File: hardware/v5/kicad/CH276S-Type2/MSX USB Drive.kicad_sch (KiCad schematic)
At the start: 11 parts, among them J1 AVR-JTAG-10, J2 Conn_02x08_Odd_Even, SW1 SK12D07VG4, U1 EPM7064STC44-7, U2 SST39SF040

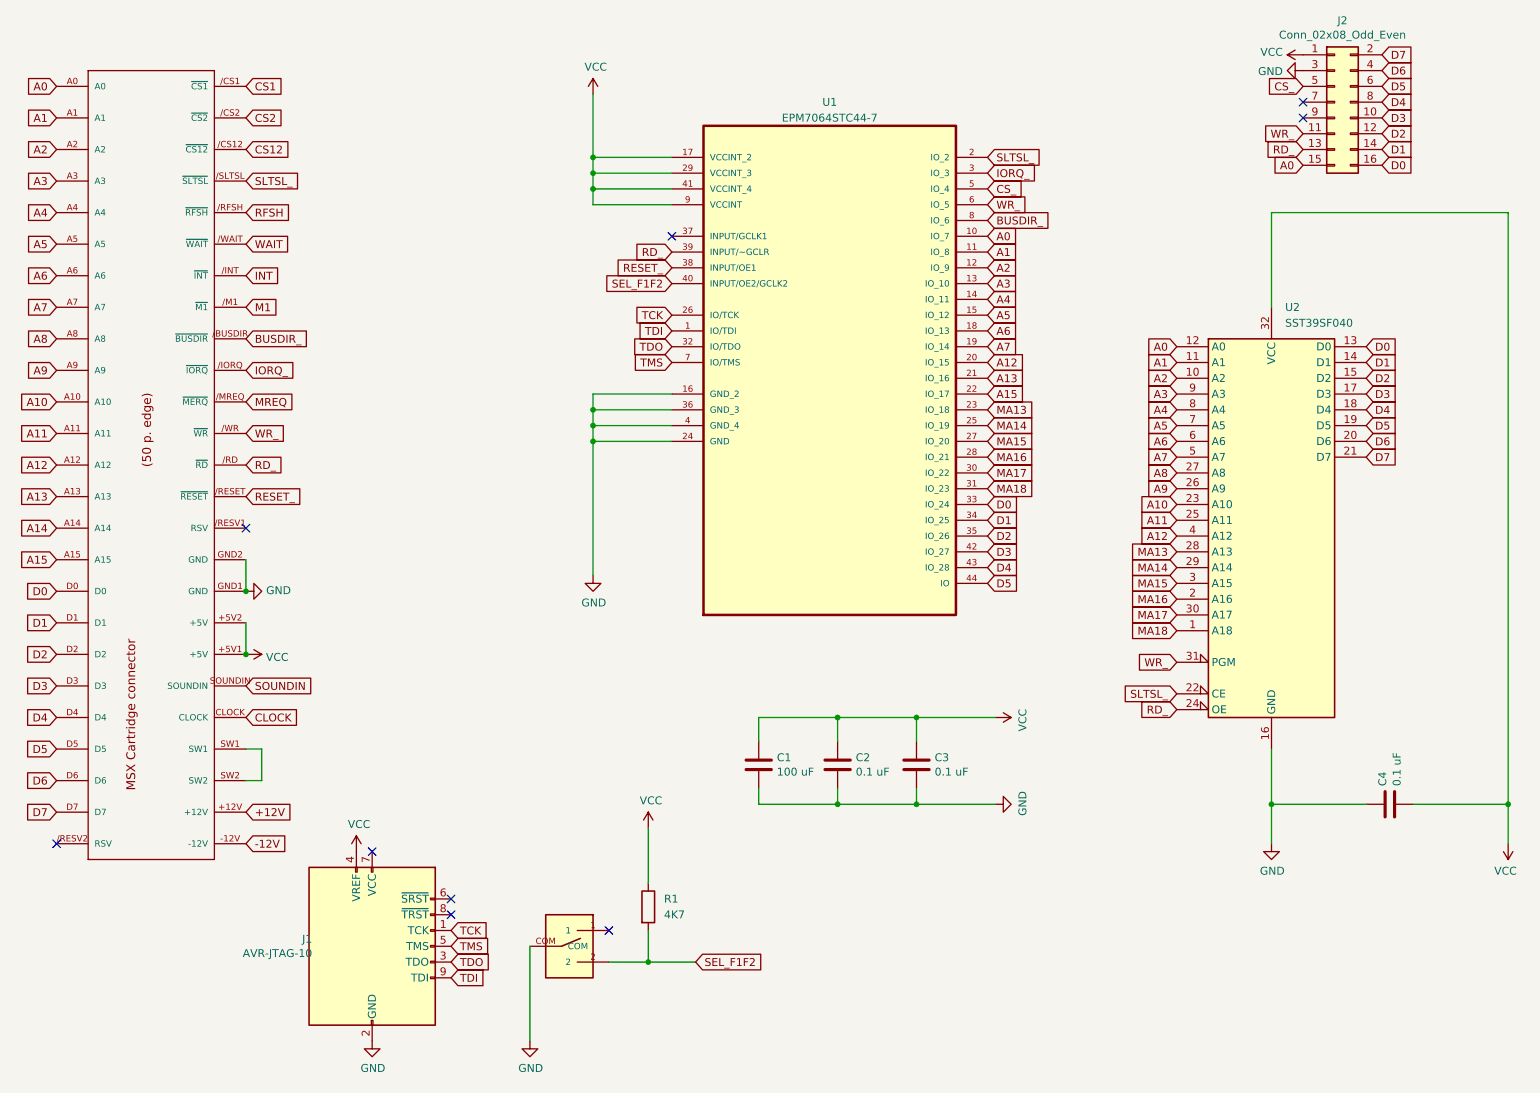
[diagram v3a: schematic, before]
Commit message: fix flash tool, adjustments to v5 pcbs, tests with fusion-c
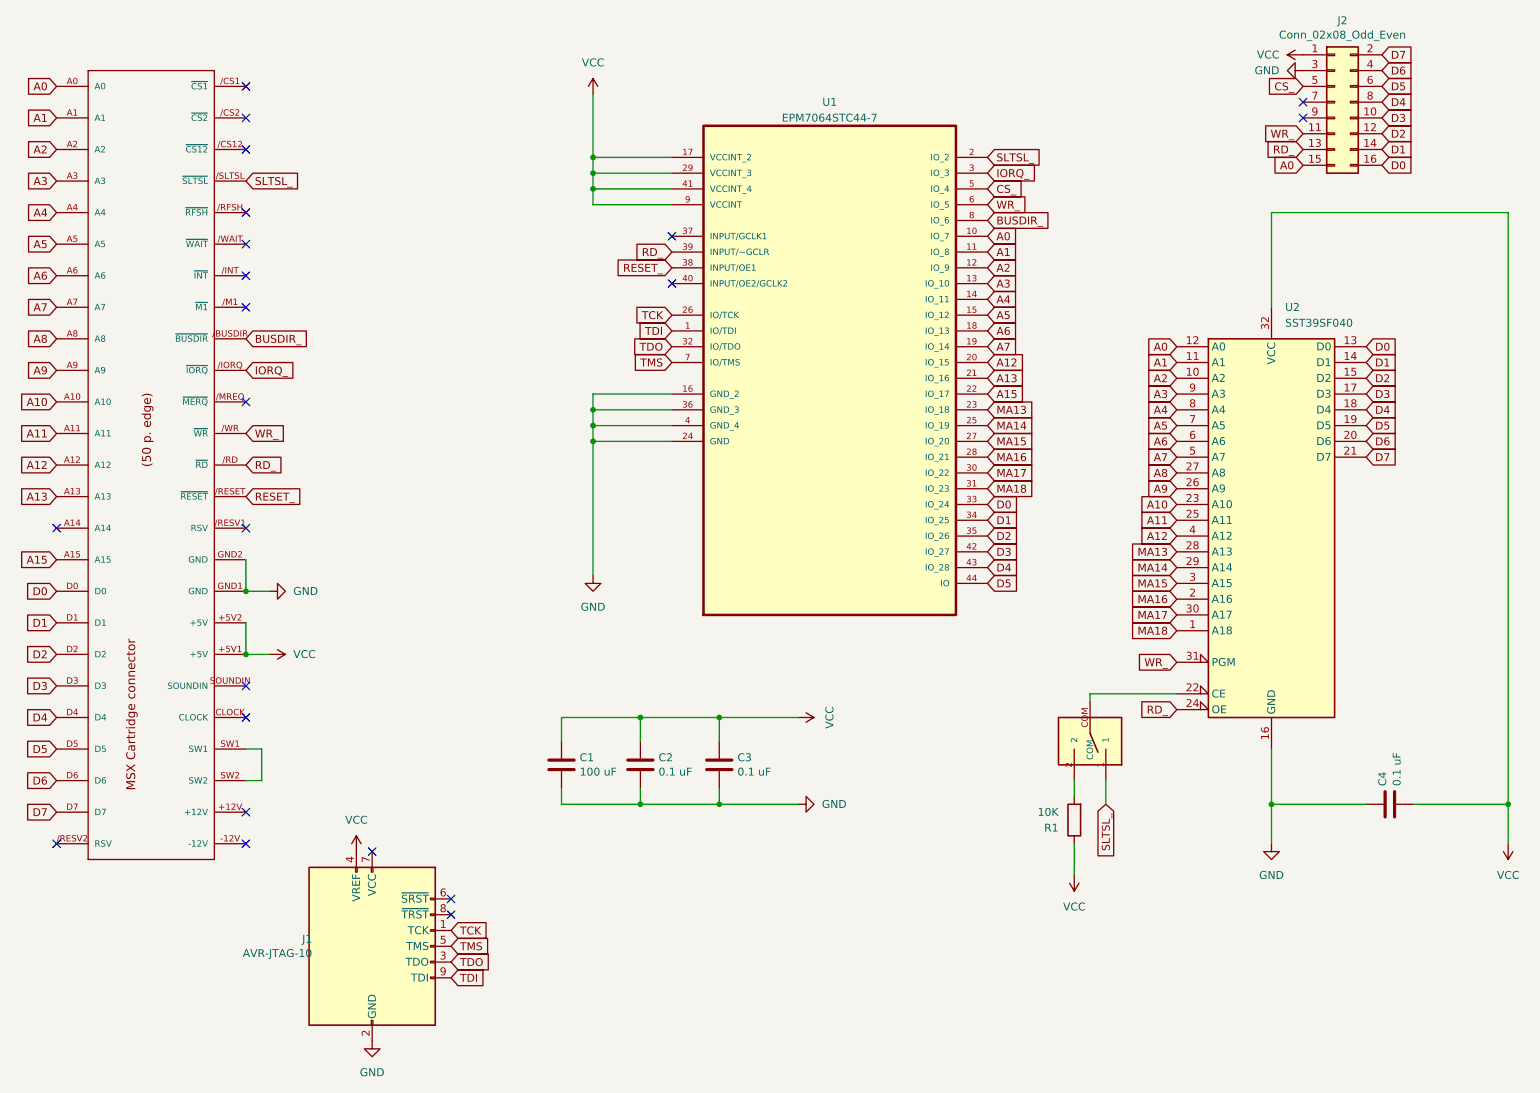
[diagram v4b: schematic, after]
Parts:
- R1: value 4K7 -> 10K
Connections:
- net GND: no longer SW1.COM
- net SLTSL_: now also SW1.1; no longer U2.22 (CE)
- net +12V: no longer names the net of EDG1.+12V
- net -12V: no longer names the net of EDG1.-12V
- net A14: no longer names the net of EDG1.A14
- net CLOCK: no longer names the net of EDG1.CLOCK
- net CS1: no longer names the net of EDG1./CS1 (~{CS1})
- net CS12: no longer names the net of EDG1./CS12 (~{CS12})
- net CS2: no longer names the net of EDG1./CS2 (~{CS2})
- net INT: no longer names the net of EDG1./INT (~{INT})
- net M1: no longer names the net of EDG1./M1 (~{M1})
- net MREQ: no longer names the net of EDG1./MREQ (~{MERQ})
- net RFSH: no longer names the net of EDG1./RFSH (~{RFSH})
- net SEL_F1F2: no longer names the net of R1.2, SW1.2
- net SEL_F1F2: no longer U1.40 (INPUT/OE2/GCLK2)
- net SOUNDIN: no longer names the net of EDG1.SOUNDIN
- net WAIT: no longer names the net of EDG1./WAIT (~{WAIT})
- new net: SW1.COM, U2.22 (CE)
- no-connect marks 9 -> 22
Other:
- moved on the sheet: C1, C2, C3, R1
